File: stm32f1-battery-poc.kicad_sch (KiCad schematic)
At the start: 88 parts, among them J1 Conn_02x07_Odd_Even, J2 Conn_01x02, J3 Conn_01x02, M1 Motor_3_Phases, Q1 Q_NMOS, Q2 Q_NMOS, SW1 SW_Push, SW2 SW_Push, SW3 SW_Push, SW4 SW_SPST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

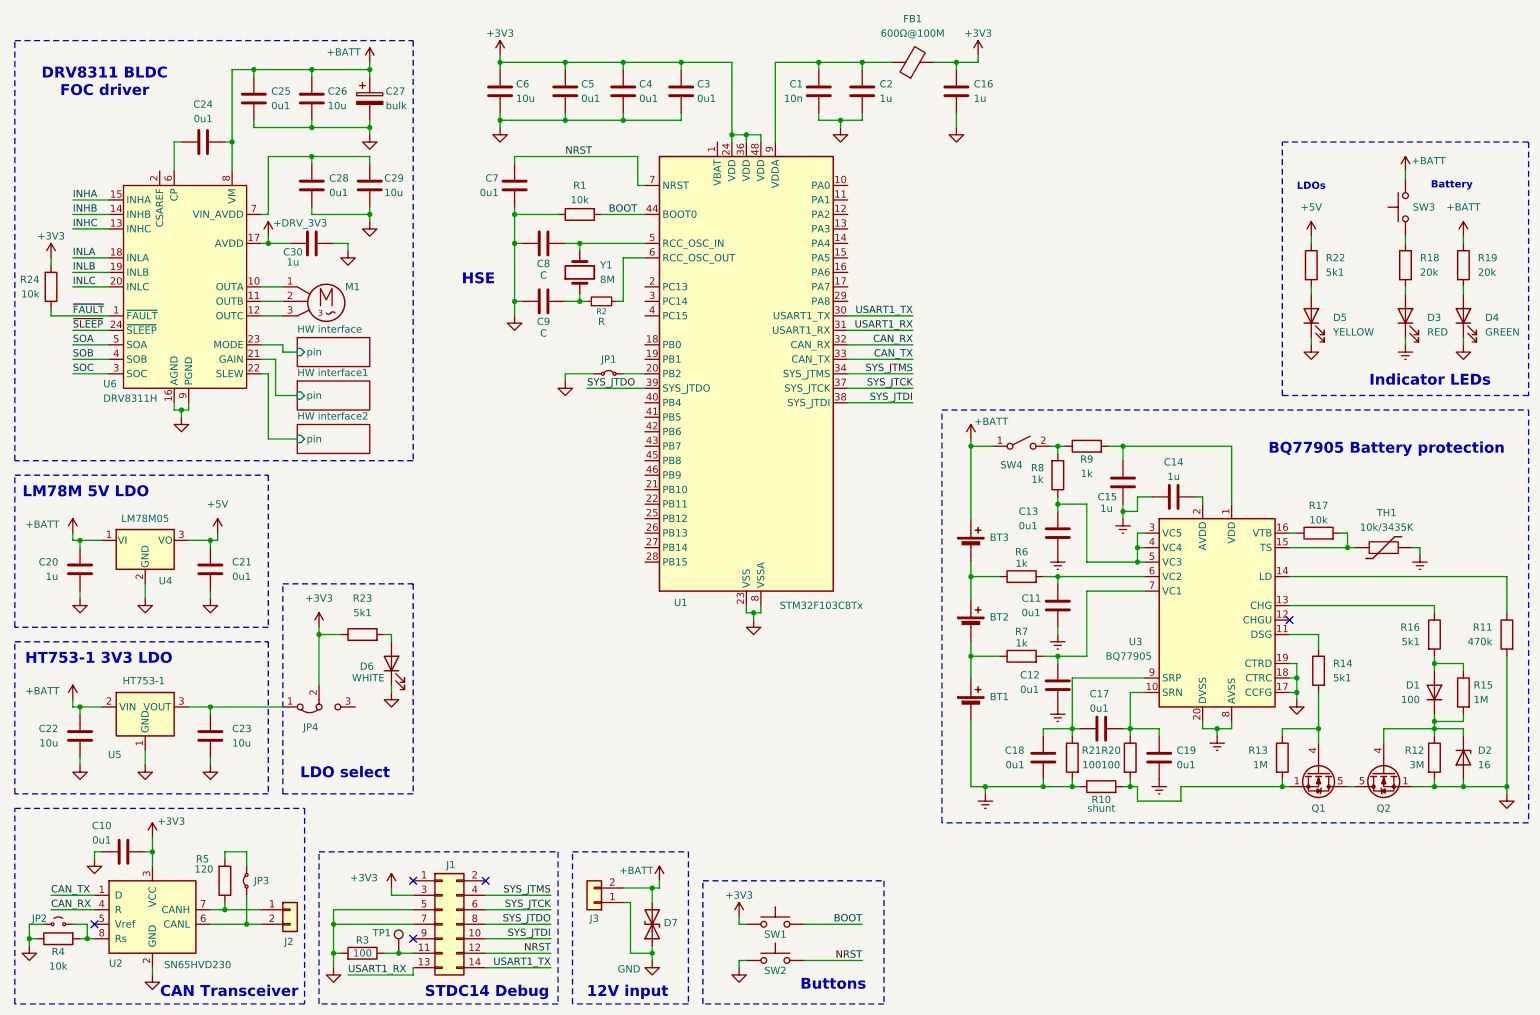
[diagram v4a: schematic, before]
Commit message: schem: import QRE1113 reflective sensor from motor-power-poc
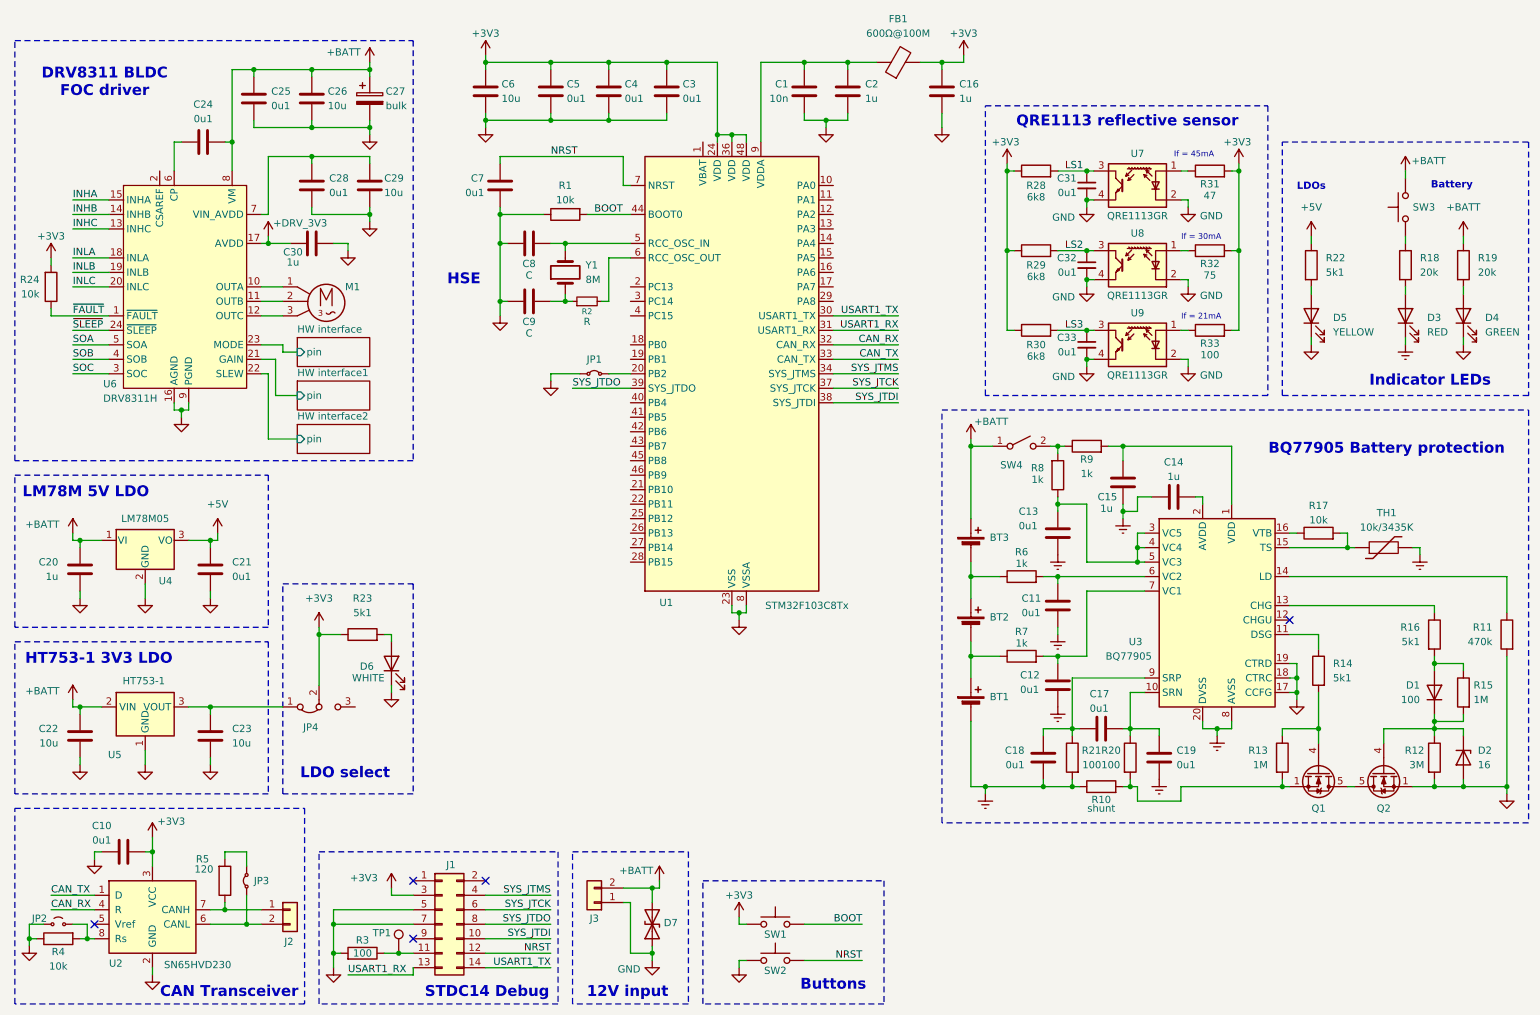
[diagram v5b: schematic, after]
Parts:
- added C31, C32, C33: 0u1, Capacitor_SMD:C_0402_1005Metric, symbol Device:C_Small
- added R28, R29, R30: 6k8, Resistor_SMD:R_0603_1608Metric, symbol Device:R
- added R31: 47, Resistor_SMD:R_0603_1608Metric, symbol Device:R
- added R32: 75, Resistor_SMD:R_0603_1608Metric, symbol Device:R
- added R33: 100, Resistor_SMD:R_0603_1608Metric, symbol Device:R
- added U7, U8, U9: QRE1113GR, OptoDevice:OnSemi_CASE100CY, symbol Sensor_Proximity:QRE1113GR
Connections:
- net +3V3: now also R28.1, R29.1, R30.1, R31.2, R32.2, R33.2
- net EPAD: now also C31.2, C32.2, C33.2, U7.2 (K), U7.4, U8.2 (K), U8.4, U9.2 (K), U9.4
- new net: R31.1, U7.1 (A)
- new net: R32.1, U8.1 (A)
- new net: R33.1, U9.1 (A)
- new net LS1: C31.1, R28.2, U7.3
- new net LS2: C32.1, R29.2, U8.3
- new net LS3: C33.1, R30.2, U9.3
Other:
- note added: "If = 21mA"
- note added: "If = 30mA"
- note added: "If = 45mA"
- note added: "QRE1113 reflective sensor"
- moved on the sheet: C1, C16, C2, C3, C4, C5, C6, C7, C8, C9, FB1, JP1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

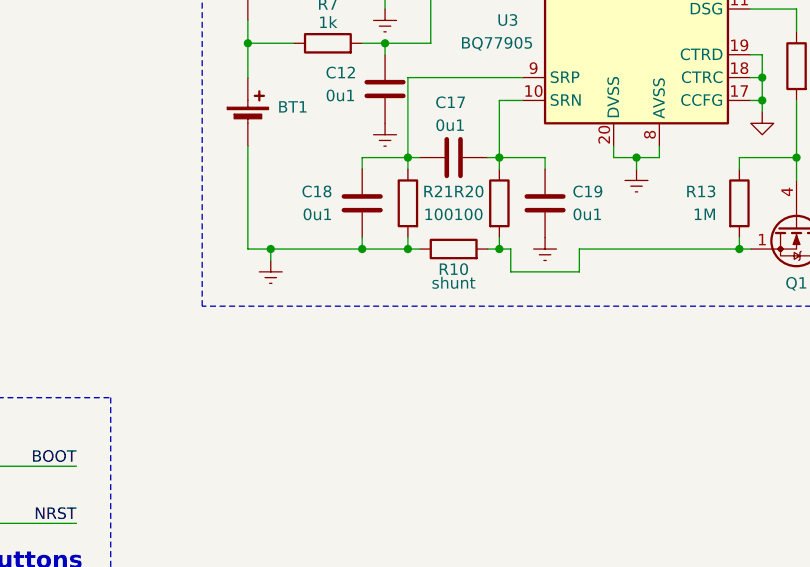
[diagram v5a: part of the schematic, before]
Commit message: schem: add BQ77905 shunt resistor value
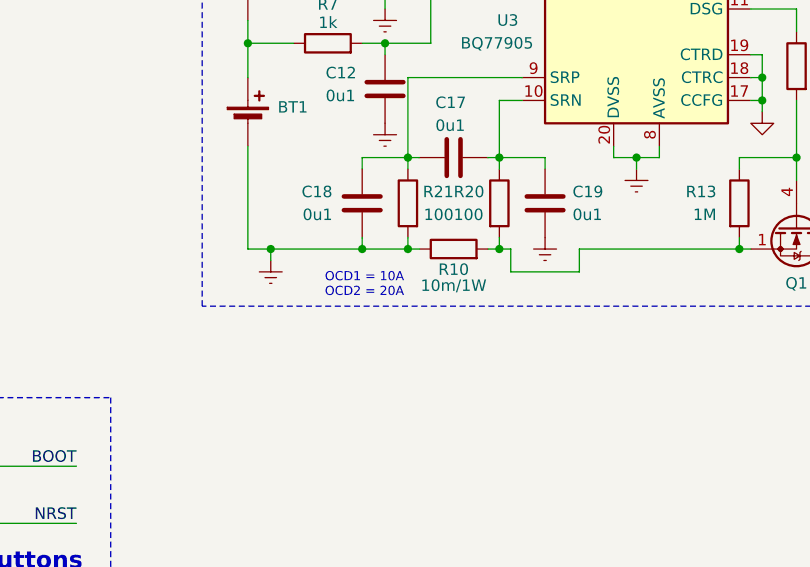
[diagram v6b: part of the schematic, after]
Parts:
- R10: value shunt -> 10m/1W
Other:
- note added: "OCD1 = 10A OCD2 = 20A"
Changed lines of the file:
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@@
 		)
 	)
+	(text "OCD1 = 10A\nOCD2 = 20A"
+		(exclude_from_sim no)
+		(at 197.104 160.274 0)
+		(effects
+			(font
+				(size 1.016 1.016)
+				(thickness 0.127)
+				(color 132 132 132 1)
+			)
+		)
+	)
 	(text "STDC14 Debug"
 		(exclude_from_sim no)
@@
 			)
 		)
-		(property "Value" "shunt"
-			(at 207.01 160.02 90)
+		(property "Value" "10m/1W"
+			(at 207.01 160.274 90)
 			(effects
 				(font

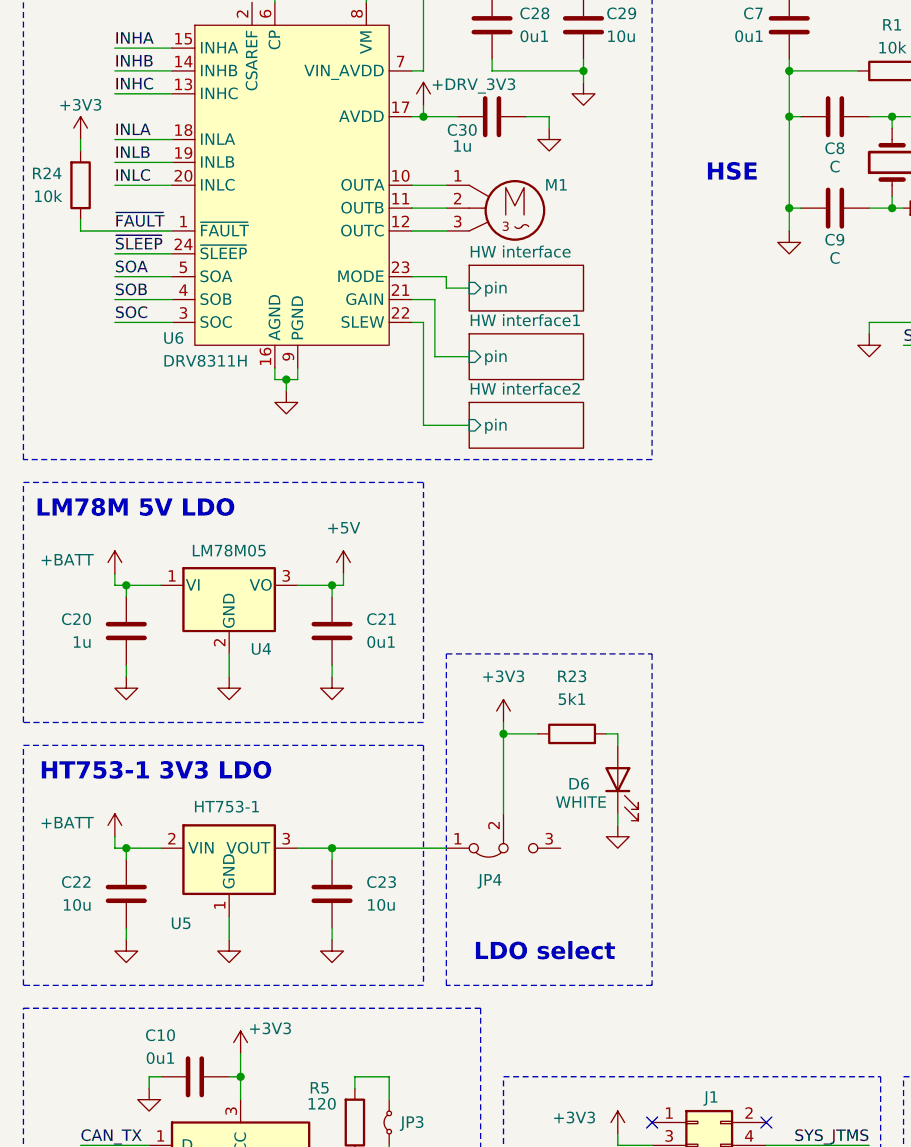
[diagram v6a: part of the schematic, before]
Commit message: schem: clean up LDO select
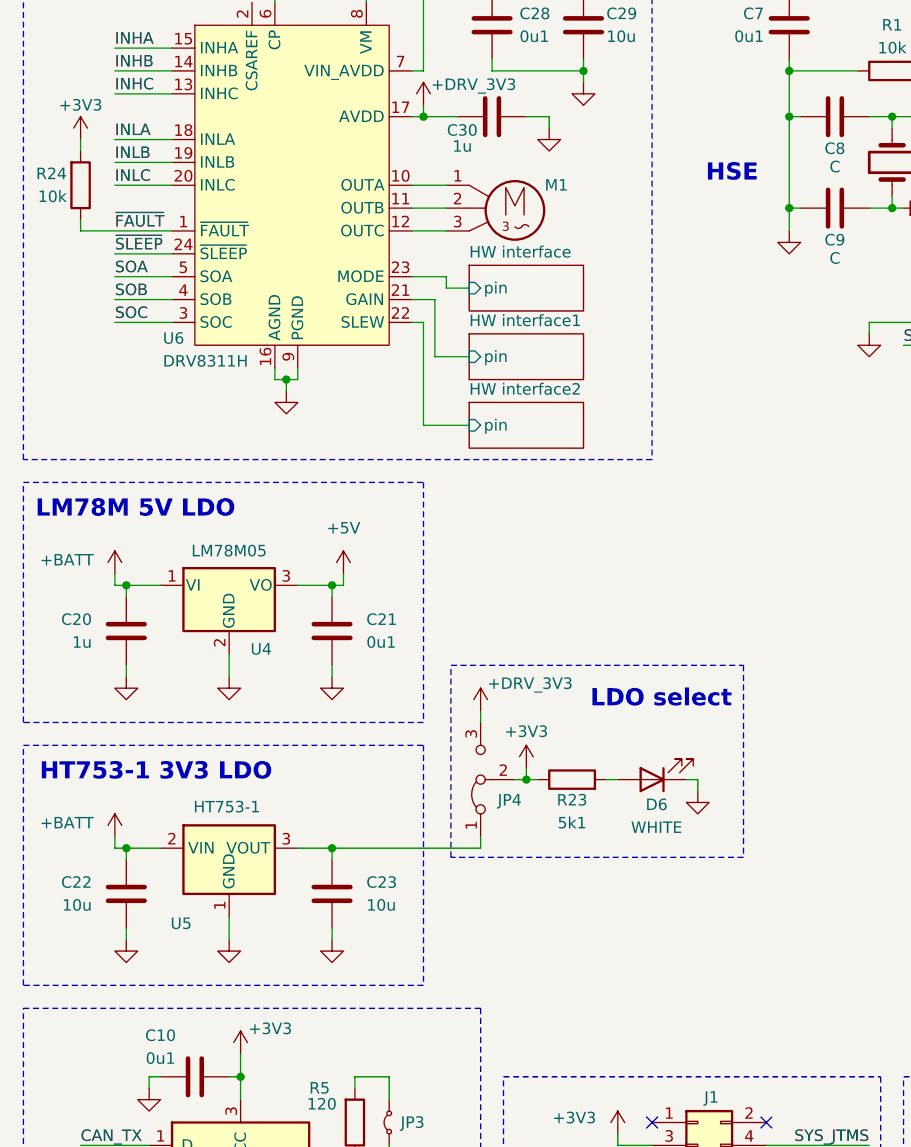
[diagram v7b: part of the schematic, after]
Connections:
- net +DRV_3V3: now also JP4.3 (B)
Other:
- moved on the sheet: D6, JP4, R23

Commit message: schem: add DRV8311 missing power inputs
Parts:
- added C34: 10n, symbol Device:C
- added C35, C36: 1u, symbol Device:C
- added FB2: 600Ω@100M, symbol Device:FerriteBead_Small
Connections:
- net +3V3: now also C36.1, FB2.2
- net +BATT: now also C28.2, C29.2, U6.7 (VIN_AVDD)
- net EPAD: now also C34.2, C35.2, C36.2
- net at U6.2 (CSAREF): now also C34.1, C35.1, FB2.1
